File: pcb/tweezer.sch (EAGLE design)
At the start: 33 parts, among them IC1 AD7995, IC2 TS507CLT, IC3 TS507CLT, IC5 ESDA6V1SC5, IC6 AT24CS04-SOT23

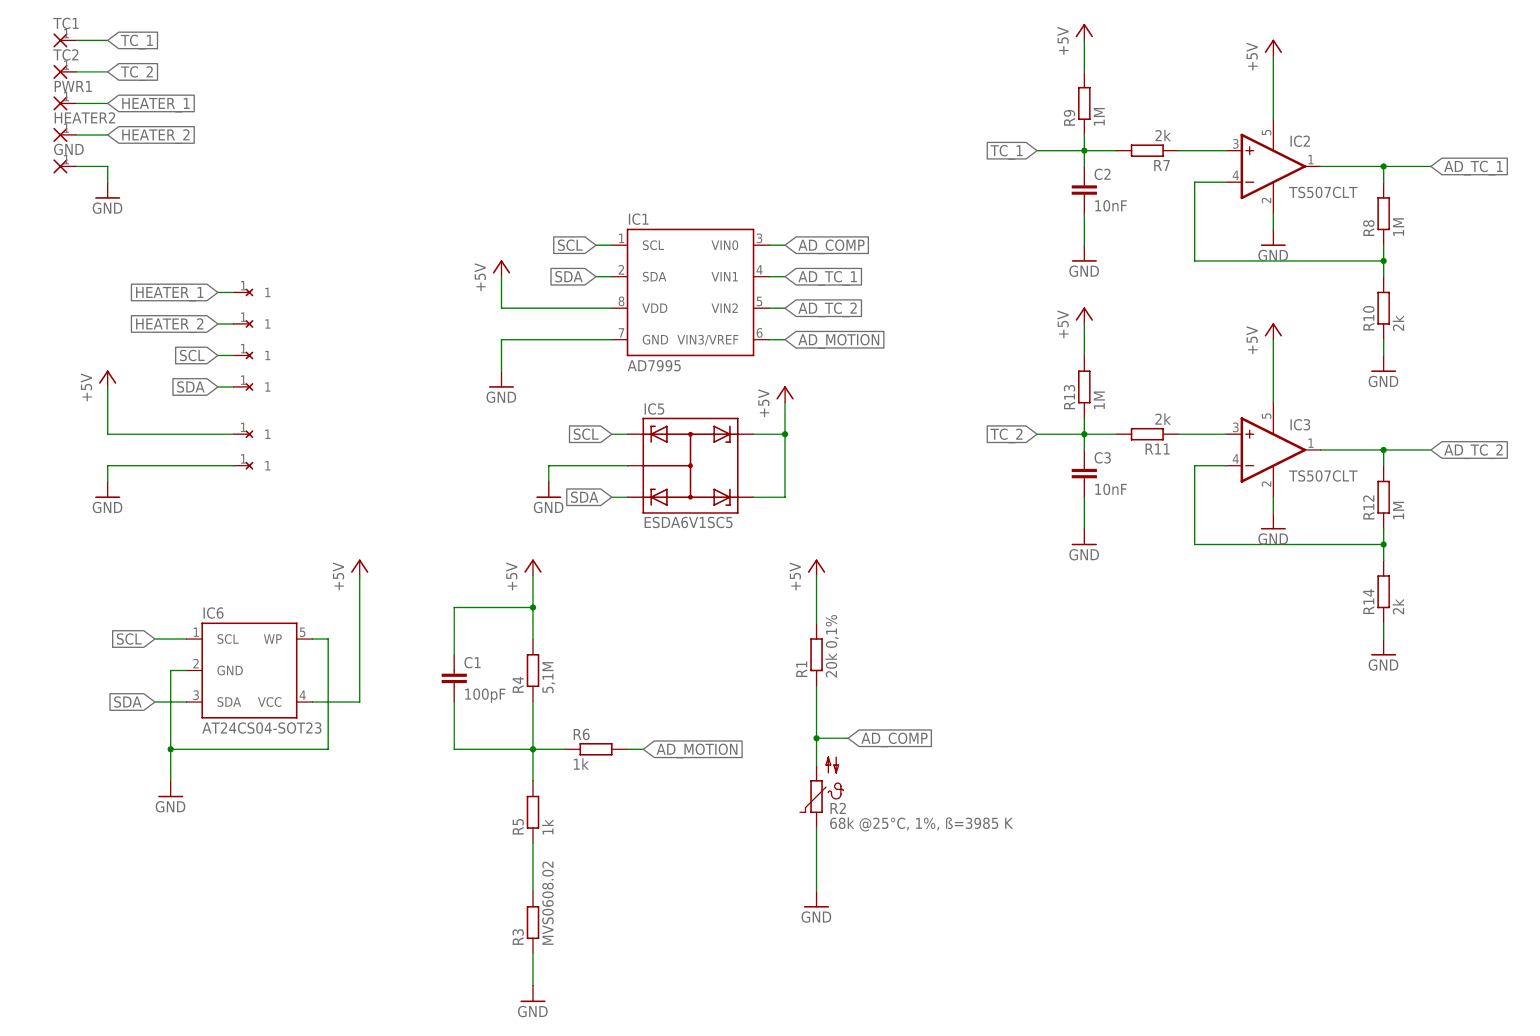
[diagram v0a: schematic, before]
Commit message: shottky diode added to iron/tweezer
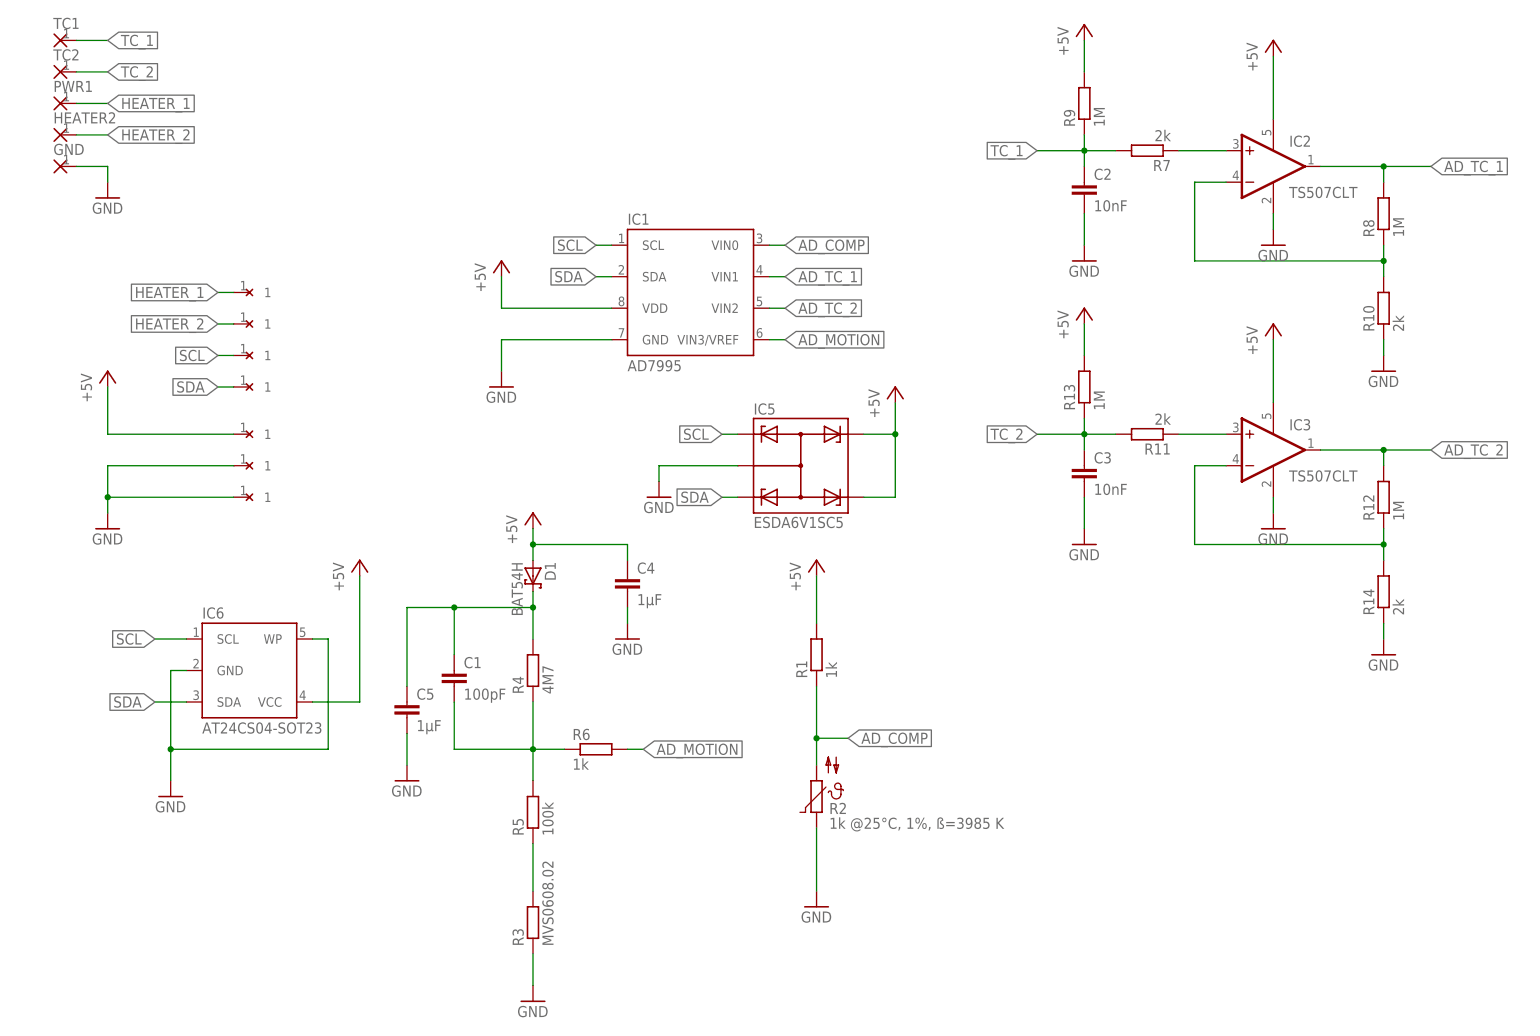
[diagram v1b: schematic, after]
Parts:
- added C4, C5: 1µF, common:C-EU0603
- added D1: BAT54H, solderpi:BAT54H
- added U$1: WIREPAD, solderpi:WIREPAD
- R1: value 20k 0,1% -> 1k
- R2: value 68k @25°C, 1%, ß=3985 K -> 1k @25°C, 1%, ß=3985 K
- R4: value 5,1M -> 4M7
- R5: value 1k -> 100k
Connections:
- new net N$1: C1.1, C5.1, D1.C, R4.2
- net +5V: now also C4.1, D1.A; no longer C1.1, R4.2
- net GND: now also C4.2, C5.2, U$1.1
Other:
- moved on the sheet: IC5

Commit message: iron tweezer updated
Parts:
- C1: OC_DIGIKEY (none) -> 478-7926-1-ND; OC_MOUSER 80-C0805C101J5RAUTO -> (none)
- C2, C3: OC_DIGIKEY (none) -> 478-6209-1-ND
- IC1: OC_DIGIKEY AD7995YRJZ-0500RL7CT-ND -> AD7995YRJZ-1500RL7CT-ND
- IC5: OC_DIGIKEY AD7995YRJZ-0500RL7CT-ND -> 497-7748-1-ND
- R1: OC_DIGIKEY (none) -> P1.0KDBCT-ND
- R10, R11, R14, R7: value 2k -> 2k 0.1%; OC_DIGIKEY (none) -> TNP2.00KAACT-ND
- R12, R13, R8, R9: value 1M -> 1M 0,1%; OC_DIGIKEY (none) -> YAG4498CT-ND
- R2: OC_DIGIKEY (none) -> P123687CT-ND
- R4: OC_DIGIKEY (none) -> 311-4.70MHRCT-ND
- R5: OC_DIGIKEY (none) -> RMCF0603FT100KCT-ND
- R6: OC_DIGIKEY (none) -> RMCF0603FT1K00CT-ND
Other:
- moved on the sheet: IC1, IC5
